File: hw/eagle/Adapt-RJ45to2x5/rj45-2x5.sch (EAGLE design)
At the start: 8 parts, among them P11 SOLPAD035, P21 SOLPAD035

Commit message: update of pcbs. save work
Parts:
- added JP4: BMS ribbon, pinhead:PINHD-2X5_KEYED
- added JP5: M-RESET, pinhead:PINHD-1X1
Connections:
- new net N$2: JP4.10, JP6.10
- net +12V: now also JP4.1, JP4.7, JP4.8
- net CANH: now also JP4.4
- net CANL: now also JP4.3
- net GNDA: now also JP4.2, JP4.5, JP4.9
- net MASTER-RESET-SYS: now also JP4.6, JP5.1
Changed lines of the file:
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@@
 <setting verticaltext="up"/>
 </settings>
-<grid distance="0.1" unitdist="inch" unit="inch" style="lines" multiple="1" display="no" altdistance="0.01" altunitdist="inch" altunit="inch"/>
+<grid distance="0.025" unitdist="inch" unit="inch" style="lines" multiple="1" display="no" altdistance="0.01" altunitdist="inch" altunit="inch"/>
 <layers>
 <layer number="1" name="Top" color="4" fill="1" visible="no" active="no"/>
@@
 <layer number="91" name="Nets" color="2" fill="1" visible="yes" active="yes"/>
 <layer number="92" name="Busses" color="1" fill="1" visible="yes" active="yes"/>
-<layer number="93" name="Pins" color="2" fill="1" visible="no" active="yes"/>
+<layer number="93" name="Pins" color="2" fill="1" visible="yes" active="yes"/>
 <layer number="94" name="Symbols" color="4" fill="1" visible="yes" active="yes"/>
 <layer number="95" name="Names" color="7" fill="1" visible="yes" active="yes"/>
@@
 <part name="JP2" library="pinhead" deviceset="PINHD-1X1" device="" value="+12V"/>
 <part name="JP3" library="pinhead" deviceset="PINHD-1X1" device="" value="GND"/>
+<part name="JP4" library="pinhead" deviceset="PINHD-2X5_KEYED" device="" value="BMS ribbon"/>
+<part name="JP5" library="pinhead" deviceset="PINHD-1X1" device="" value="M-RESET"/>
 </parts>
 <sheets>
@@
 <text x="28.575" y="53.975" size="1.778" layer="91" rot="R180">CAN BUS PLUS</text>
 <text x="47.625" y="89.535" size="1.778" layer="91" rot="R270">PASS-THRU</text>
-<text x="43.18" y="39.37" size="1.778" layer="91" rot="R90">CAN BUS PLUS</text>
-<text x="52.07" y="38.1" size="1.778" layer="91" rot="R90">CAN BUS MINUS</text>
+<text x="43.18" y="48.895" size="1.778" layer="91" rot="R90">CAN BUS PLUS</text>
+<text x="52.705" y="48.26" size="1.778" layer="91" rot="R90">CAN BUS MINUS</text>
 <text x="66.675" y="49.53" size="1.778" layer="91" rot="R90">CAN-H</text>
 <text x="60.325" y="50.165" size="1.778" layer="91" rot="R90">CAN-L</text>
@@
 <instance part="JP2" gate="G$1" x="79.375" y="108.585"/>
 <instance part="JP3" gate="G$1" x="80.01" y="91.44"/>
+<instance part="JP4" gate="G$1" x="85.09" y="32.385" rot="R180"/>
+<instance part="JP5" gate="G$1" x="94.615" y="85.725"/>
 </instances>
 <busses>
@@
 <wire x1="77.47" y1="91.44" x2="53.975" y2="91.44" width="0.1524" layer="91"/>
 <junction x="53.975" y="91.44"/>
+<pinref part="JP4" gate="G$1" pin="2"/>
+<wire x1="36.83" y1="23.495" x2="80.01" y2="23.495" width="0.1524" layer="91"/>
+<wire x1="80.01" y1="23.495" x2="80.01" y2="27.305" width="0.1524" layer="91"/>
+<junction x="36.83" y="23.495"/>
+<wire x1="80.01" y1="23.495" x2="95.25" y2="23.495" width="0.1524" layer="91"/>
+<wire x1="95.25" y1="23.495" x2="95.25" y2="32.385" width="0.1524" layer="91"/>
+<junction x="80.01" y="23.495"/>
+<pinref part="JP4" gate="G$1" pin="5"/>
+<wire x1="95.25" y1="32.385" x2="87.63" y2="32.385" width="0.1524" layer="91"/>
+<wire x1="95.25" y1="32.385" x2="95.25" y2="37.465" width="0.1524" layer="91"/>
+<junction x="95.25" y="32.385"/>
+<pinref part="JP4" gate="G$1" pin="9"/>
+<wire x1="95.25" y1="37.465" x2="87.63" y2="37.465" width="0.1524" layer="91"/>
 </segment>
 </net>
@@
 <wire x1="76.835" y1="108.585" x2="44.45" y2="108.585" width="0.1524" layer="91"/>
 <junction x="44.45" y="108.585"/>
+<pinref part="JP4" gate="G$1" pin="1"/>
+<wire x1="31.75" y1="21.59" x2="74.93" y2="21.59" width="0.1524" layer="91"/>
+<wire x1="74.93" y1="21.59" x2="87.63" y2="21.59" width="0.1524" layer="91"/>
+<wire x1="87.63" y1="21.59" x2="87.63" y2="27.305" width="0.1524" layer="91"/>
+<junction x="31.75" y="21.59"/>
+<pinref part="JP4" gate="G$1" pin="7"/>
+<pinref part="JP4" gate="G$1" pin="8"/>
+<wire x1="87.63" y1="34.925" x2="80.01" y2="34.925" width="0.1524" layer="91"/>
+<wire x1="80.01" y1="34.925" x2="74.93" y2="34.925" width="0.1524" layer="91"/>
+<wire x1="74.93" y1="34.925" x2="74.93" y2="21.59" width="0.1524" layer="91"/>
+<junction x="80.01" y="34.925"/>
+<junction x="74.93" y="21.59"/>
 </segment>
 </net>
@@
 <wire x1="78.105" y1="62.865" x2="61.595" y2="62.865" width="0.1524" layer="91"/>
 <junction x="61.595" y="62.865"/>
+<wire x1="61.595" y1="29.845" x2="78.105" y2="29.845" width="0.1524" layer="91"/>
+<wire x1="78.105" y1="29.845" x2="78.105" y2="31.115" width="0.1524" layer="91"/>
+<junction x="61.595" y="29.845"/>
+<pinref part="JP4" gate="G$1" pin="3"/>
+<wire x1="78.105" y1="31.115" x2="87.63" y2="31.115" width="0.1524" layer="91"/>
+<wire x1="87.63" y1="31.115" x2="87.63" y2="29.845" width="0.1524" layer="91"/>
 </segment>
 </net>
@@
 <wire x1="78.105" y1="65.405" x2="67.945" y2="65.405" width="0.1524" layer="91"/>
 <junction x="67.945" y="65.405"/>
+<pinref part="JP4" gate="G$1" pin="4"/>
+<wire x1="67.945" y1="28.575" x2="80.01" y2="28.575" width="0.1524" layer="91"/>
+<wire x1="80.01" y1="28.575" x2="80.01" y2="29.845" width="0.1524" layer="91"/>
+<junction x="67.945" y="28.575"/>
 </segment>
 </net>
@@
 <wire x1="26.67" y1="60.96" x2="8.255" y2="60.96" width="0.1524" layer="91"/>
 <wire x1="8.255" y1="60.96" x2="8.255" y2="32.385" width="0.1524" layer="91"/>
-<wire x1="8.255" y1="60.96" x2="8.255" y2="94.615" width="0.1524" layer="91"/>
+<wire x1="8.255" y1="60.96" x2="8.255" y2="89.535" width="0.1524" layer="91"/>
 <junction x="8.255" y="60.96"/>
 <pinref part="JP8" gate="G$1" pin="8"/>
+<wire x1="8.255" y1="89.535" x2="8.255" y2="94.615" width="0.1524" layer="91"/>
 <wire x1="8.255" y1="94.615" x2="26.67" y2="94.615" width="0.1524" layer="91"/>
-</segment>
-</net>
+<wire x1="24.13" y1="32.385" x2="24.13" y2="33.655" width="0.1524" layer="91"/>
+<junction x="24.13" y="32.385"/>
+<pinref part="JP4" gate="G$1" pin="6"/>
+<wire x1="24.13" y1="33.655" x2="80.01" y2="33.655" width="0.1524" layer="91"/>
+<wire x1="80.01" y1="33.655" x2="80.01" y2="32.385" width="0.1524" layer="91"/>
+<pinref part="JP5" gate="G$1" pin="1"/>
+<wire x1="92.075" y1="85.725" x2="37.465" y2="85.725" width="0.1524" layer="91"/>
+<wire x1="37.465" y1="85.725" x2="37.465" y2="89.535" width="0.1524" layer="91"/>
+<wire x1="37.465" y1="89.535" x2="8.255" y2="89.535" width="0.1524" layer="91"/>
+<junction x="8.255" y="89.535"/>
+</segment>
+</net>
+<net name="N$2" class="0">
+<segment>
+<pinref part="JP6" gate="G$1" pin="10"/>
+<wire x1="24.13" y1="37.465" x2="24.13" y2="38.735" width="0.1524" layer="91"/>
+<pinref part="JP4" gate="G$1" pin="10"/>
+<wire x1="24.13" y1="38.735" x2="80.01" y2="38.735" width="0.1524" layer="91"/>
+<wire x1="80.01" y1="38.735" x2="80.01" y2="37.465" width="0.1524" layer="91"/>
+</segment>
+</net>

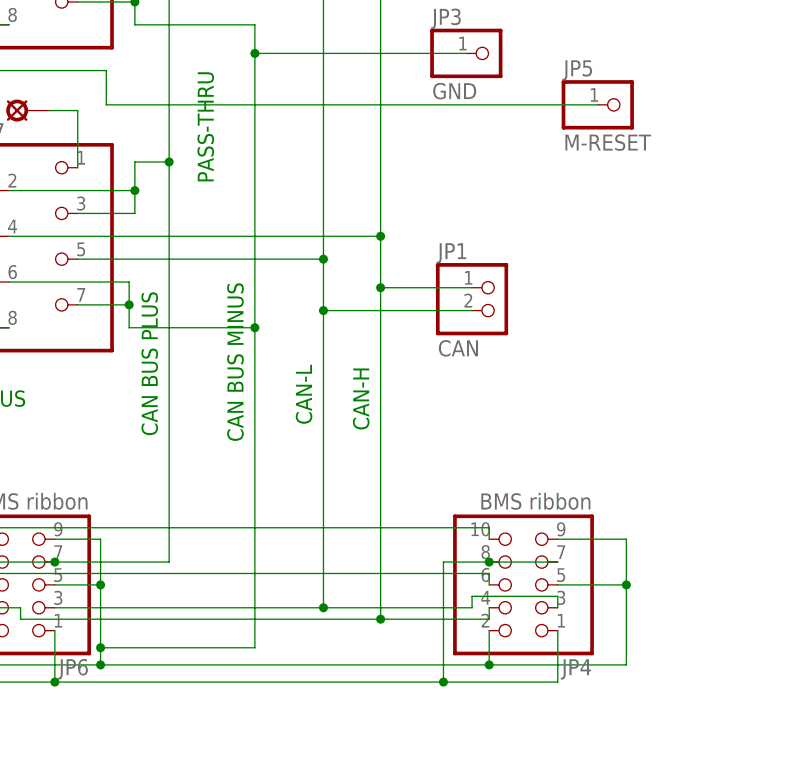
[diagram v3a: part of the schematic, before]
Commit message: 14921 pcb updates. DUMP 3 pin, plus VOred pin added
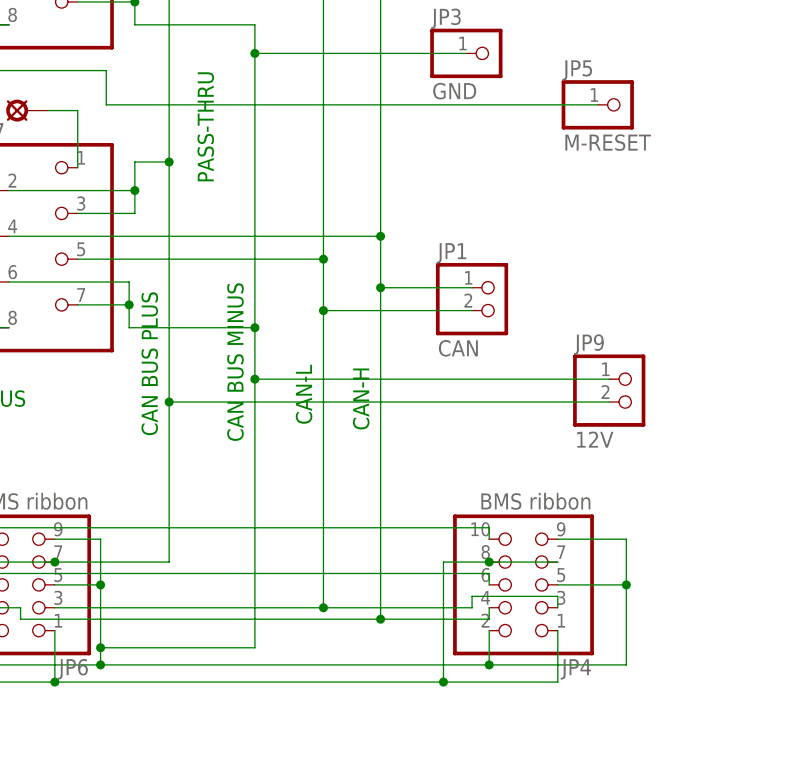
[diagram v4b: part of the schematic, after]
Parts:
- added JP9: 12V, pinhead:PINHD-1X2
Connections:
- net +12V: now also JP9.2
- net GNDA: now also JP9.1
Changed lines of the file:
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@@
 <part name="JP4" library="pinhead" deviceset="PINHD-2X5_KEYED" device="" value="BMS ribbon"/>
 <part name="JP5" library="pinhead" deviceset="PINHD-1X1" device="" value="M-RESET"/>
+<part name="JP9" library="pinhead" deviceset="PINHD-1X2" device="" value="12V"/>
 </parts>
 <sheets>
@@
 <instance part="JP4" gate="G$1" x="85.09" y="32.385" rot="R180"/>
 <instance part="JP5" gate="G$1" x="94.615" y="85.725"/>
+<instance part="JP9" gate="G$1" x="95.885" y="52.705"/>
 </instances>
 <busses>
@@
 <pinref part="JP6" gate="G$1" pin="9"/>
 <pinref part="GND10" gate="1" pin="GNDA"/>
-<wire x1="53.975" y1="60.96" x2="53.975" y2="25.4" width="0.1524" layer="91"/>
+<wire x1="53.975" y1="60.96" x2="53.975" y2="55.245" width="0.1524" layer="91"/>
 <junction x="53.975" y="60.96"/>
 <pinref part="JP3" gate="G$1" pin="1"/>
+<wire x1="53.975" y1="55.245" x2="53.975" y2="25.4" width="0.1524" layer="91"/>
 <wire x1="77.47" y1="91.44" x2="53.975" y2="91.44" width="0.1524" layer="91"/>
 <junction x="53.975" y="91.44"/>
@@
 <pinref part="JP4" gate="G$1" pin="9"/>
 <wire x1="95.25" y1="37.465" x2="87.63" y2="37.465" width="0.1524" layer="91"/>
+<pinref part="JP9" gate="G$1" pin="1"/>
+<wire x1="93.345" y1="55.245" x2="53.975" y2="55.245" width="0.1524" layer="91"/>
+<junction x="53.975" y="55.245"/>
 </segment>
 </net>
@@
 <pinref part="JP7" gate="G$1" pin="2"/>
 <pinref part="JP7" gate="G$1" pin="5"/>
-<wire x1="44.45" y1="79.375" x2="44.45" y2="34.925" width="0.1524" layer="91"/>
+<wire x1="44.45" y1="79.375" x2="44.45" y2="52.705" width="0.1524" layer="91"/>
 <junction x="44.45" y="79.375"/>
 <pinref part="JP2" gate="G$1" pin="1"/>
+<wire x1="44.45" y1="52.705" x2="44.45" y2="34.925" width="0.1524" layer="91"/>
 <wire x1="76.835" y1="108.585" x2="44.45" y2="108.585" width="0.1524" layer="91"/>
 <junction x="44.45" y="108.585"/>
@@
 <junction x="80.01" y="34.925"/>
 <junction x="74.93" y="21.59"/>
+<pinref part="JP9" gate="G$1" pin="2"/>
+<wire x1="93.345" y1="52.705" x2="44.45" y2="52.705" width="0.1524" layer="91"/>
+<junction x="44.45" y="52.705"/>
 </segment>
 </net>
